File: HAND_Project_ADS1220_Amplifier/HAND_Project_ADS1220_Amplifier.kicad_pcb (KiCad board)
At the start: 2 copper layers, 30.5 x 38.1 mm, 17 parts, among them J2 Conn_01x05_Pin, J7 Conn_01x04_Pin

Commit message: Final touches
matched footprints with yuchan's PCB
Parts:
- removed Power: Conn_01x02_Pin, Connector_JST:JST_PH_B2B-PH-K_1x02_P2.00mm_Vertical
- 3.3: renamed from 5; footprint LED_SMD:LED_0603_1608Metric_Pad1.05x0.95mm_HandSolder -> LED_SMD:LED_0805_2012Metric_Pad1.15x1.40mm_HandSolder
- 5: renamed from 3.3; footprint LED_SMD:LED_0603_1608Metric_Pad1.05x0.95mm_HandSolder -> LED_SMD:LED_0805_2012Metric_Pad1.15x1.40mm_HandSolder
- C3, C4: value 15 nF -> 10nF
- R1, R2: value 330 -> 360; footprint Resistor_SMD:R_0603_1608Metric_Pad0.98x0.95mm_HandSolder -> Resistor_SMD:R_0805_2012Metric_Pad1.20x1.40mm_HandSolder
- R3, R4: value 10k -> 16k; footprint Resistor_SMD:R_0603_1608Metric_Pad0.98x0.95mm_HandSolder -> Resistor_SMD:R_0805_2012Metric_Pad1.20x1.40mm_HandSolder
- Strain Gauge: renamed from Strain Gauge Connector
- moved Strain Gauge 4.83 mm to (131.1, 91.4)
- moved R2 1.53 mm to (134.3, 73.9)
- moved C4 1.30 mm to (144.0, 82.7)
- moved C3 1.30 mm to (138.9, 82.7)
- moved 5 1.28 mm to (134.4, 75.9)
- moved J7 1.27 mm to (129.5, 68.8)
- moved ADS1220 1.27 mm to (138.4, 70.1)
- moved C1 1.27 mm to (137.2, 79.0)
- moved C2 1.27 mm to (137.2, 75.2)
- moved D1 1.27 mm to (141.7, 79.0)
- moved D2 1.27 mm to (141.8, 75.2)
- moved J2 1.27 mm to (147.3, 68.8)
- moved R3 1.25 mm to (140.9, 82.7)
- moved R4 1.12 mm to (146.1, 82.8)
- moved R1 1.03 mm to (134.3, 78.2)
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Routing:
- net Net-(J1-Pin_4): track 11.4 -> 7.64 mm
- net Net-(J1-Pin_3): track 11.4 -> 7.91 mm
- net GND: track 34.7 -> 35.2 mm
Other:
- board size 30.5 x 38.1 mm -> 30.5 x 33 mm
- board text removed: "5V"
- board text removed: "GND"

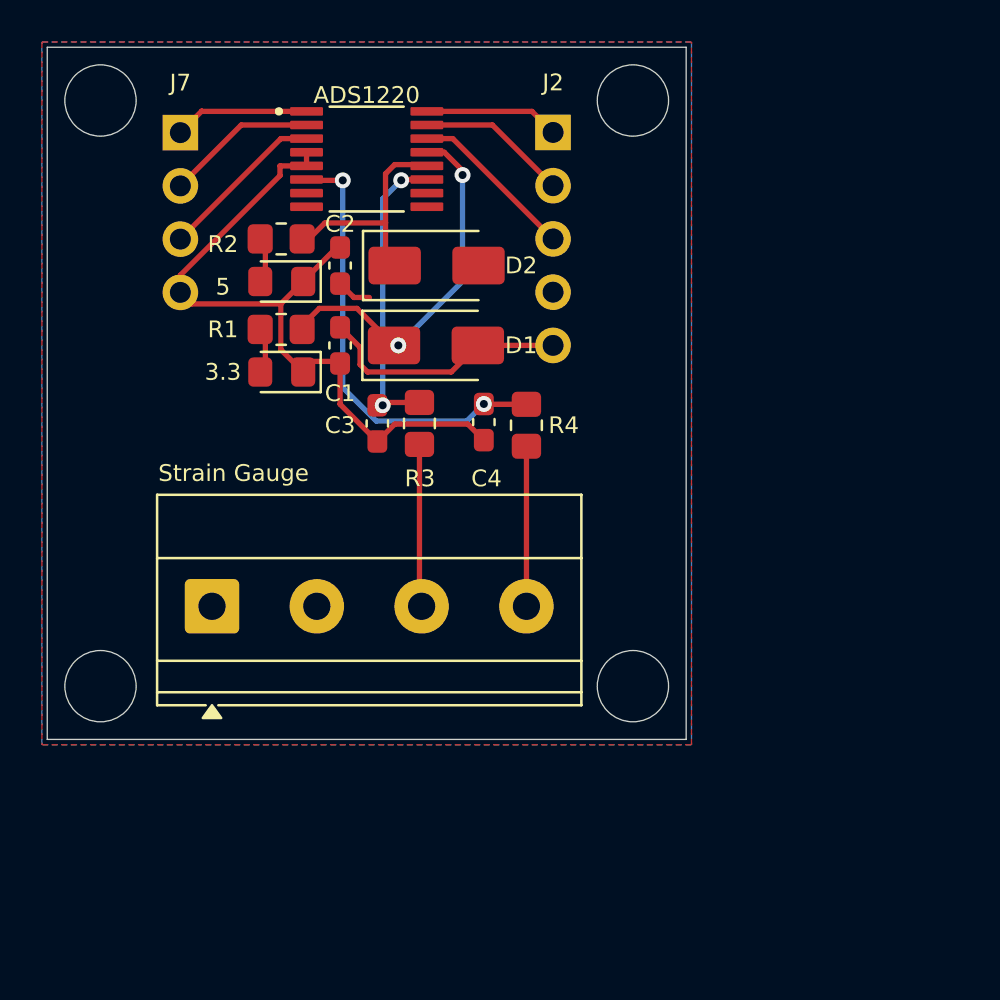
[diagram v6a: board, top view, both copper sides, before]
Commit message: new PCB no teensy
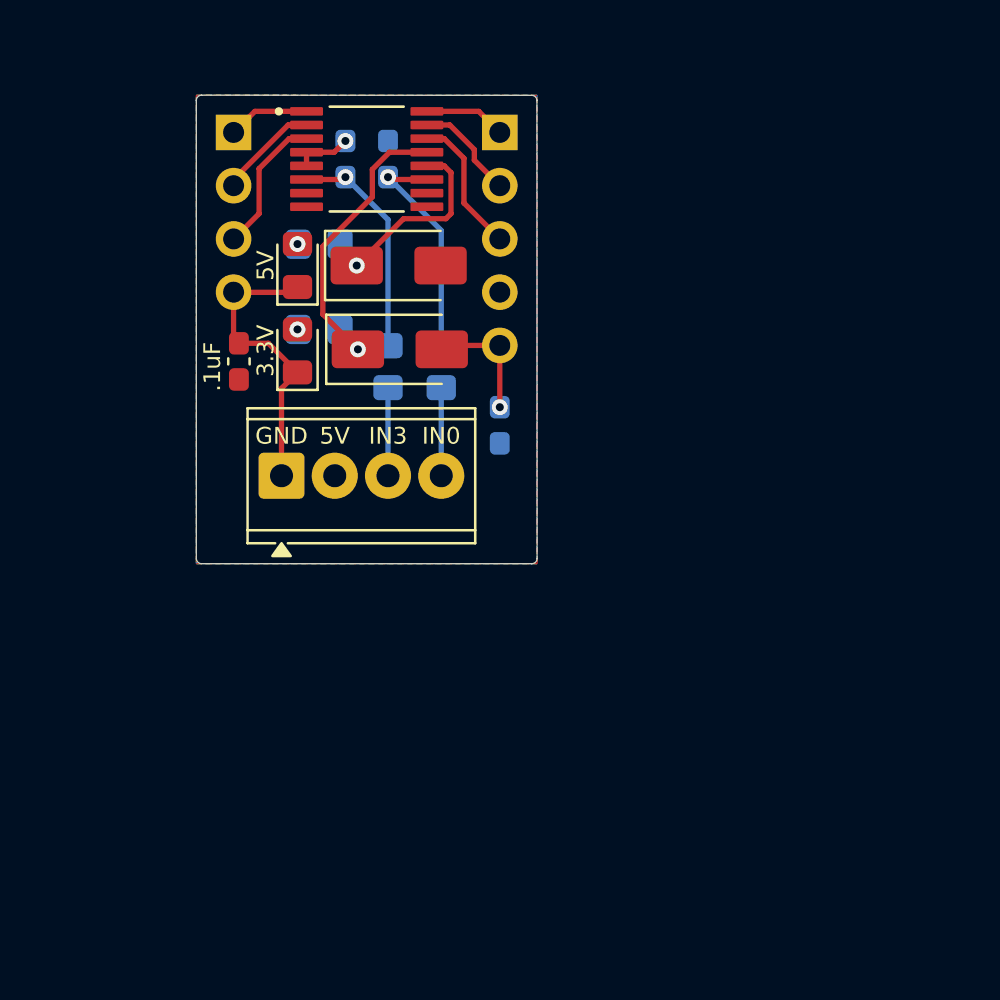
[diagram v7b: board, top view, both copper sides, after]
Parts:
- .1uF: renamed from C1; moved to B.Cu
- 10nF: renamed from C4; moved to B.Cu
- 10nF: renamed from C3; moved to B.Cu
- 16kΩ: renamed from R4; moved to B.Cu
- 16kΩ: renamed from R3; moved to B.Cu
- 360Ω: renamed from R1; moved to B.Cu
- 360Ω: renamed from R2; moved to B.Cu
- GND: renamed from Strain Gauge; footprint TerminalBlock_Phoenix:TerminalBlock_Phoenix_MKDS-1,5-4_1x04_P5.00mm_Horizontal -> TerminalBlock_Phoenix:TerminalBlock_Phoenix_MPT-0,5-4-2.54_1x04_P2.54mm_Horizontal
- moved 10nF 13.4 mm to (139.4, 70.1), turned to 90 degrees
- moved 10nF 12.7 mm to (137.4, 70.1), turned to 90 degrees
- moved .1uF 8.52 mm to (144.8, 82.8)
- moved GND 7.06 mm to (134.4, 85.2)
- moved .1uF 6.65 mm to (132.3, 79.8)
- moved 16kΩ 4.93 mm to (142.0, 80.0)
- moved 16kΩ 3.09 mm to (139.4, 80.0)
- moved J7 2.54 mm to (132.1, 68.8)
- moved J2 2.54 mm to (144.8, 68.8)
- moved 360Ω 1.83 mm to (136.2, 74.2)
- moved 360Ω 1.81 mm to (136.2, 78.2)
- moved D2 1.81 mm to (140.0, 75.2)
- moved D1 1.73 mm to (140.0, 79.2)
- moved 3.3V 1.26 mm to (135.1, 79.3), turned to 90 degrees
- moved 5V 1.07 mm to (135.1, 75.2), turned to 90 degrees
- renumbered C2 to .1uF, 3.3 to 3.3V, 5 to 5V, ADS1220 to U1
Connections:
- 10nF pad 1: /AIN3 -> /AIN0
- 10nF pad 1: /AIN0 -> /AIN3
- 16kΩ pad 2: /AIN3 -> /AIN0
- 16kΩ pad 2: /AIN0 -> /AIN3
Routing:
- net GND: track 35.2 -> 17.0 mm, vias 0 -> 1
- net /AIN3: track 21.7 -> 10.8 mm, vias 2 -> 1
- net 3.3V: track 12.0 -> 5.80 mm, vias 0 -> 1
- net Net-(J1-Pin_3): track 7.91 -> 4.21 mm
- net Net-(J1-Pin_4): track 7.64 -> 4.21 mm
- net /AIN0: track 14.2 -> 11.0 mm, vias 2 -> 1
- net /DVDD: track 17.2 -> 14.5 mm, vias 2 -> 1
- net /SCLK: track 6.46 -> 3.90 mm
- net /DIN: track 6.44 -> 3.90 mm
- net /CS: track 7.22 -> 4.86 mm
- net /DOUT: track 7.22 -> 4.98 mm
- net Net-(D3-A): track 1.79 -> 0.00 mm, vias 0 -> 1
- net Net-(D4-A): track 1.79 -> 0.00 mm, vias 0 -> 1
- net 5V: track 1.67 -> 0.00 mm
- net /DRDY: track 8.00 -> 6.71 mm
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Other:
- board size 30.5 x 33 mm -> 16.3 x 22.4 mm
- board text added: "5V"
- board text added: "IN0"
- board text added: "IN3"

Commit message: Finished new PCB without teensy integration
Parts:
- moved 10nF 0.28 mm to (139.4, 70.4)
- moved 10nF 0.28 mm to (137.4, 70.4)
- moved U1 0.25 mm to (138.4, 70.4)
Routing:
- net GND: track 17.0 -> 27.5 mm, vias 1 -> 3
- net /AVDD: track 10.1 -> 8.76 mm
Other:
- board text added: "3.3V"
- board text added: "ADS1220"
- board text added: "CLK"
- board text added: "CS"
- board text added: "DIN"
- board text added: "DOUT"
- board text added: "DRDY"
- board text added: "GND"
- board text added: "SCLK"
